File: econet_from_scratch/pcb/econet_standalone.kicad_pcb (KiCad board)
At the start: 2 copper layers, 100 x 100 mm, 24 parts, among them CON1 jtag, U1 Econet, U2 SN65C1168, U3 LM319, U4 XC9572XL, U5 MCP1700T-3302E/MB

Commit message: More progress on econet_from_scratch
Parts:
- removed CON1: jtag, Pin_Headers:Pin_Header_Straight_2x05_Pitch2.54mm
- added C7: 100n, Capacitors_SMD:C_0805_HandSoldering, F.Cu at (166.1, 52.1)
- added EXT: ext, Pin_Headers:Pin_Header_Straight_2x05_Pitch2.54mm, F.Cu at (150.4, 75.9)
- added JTAG: jtag, Pin_Headers:Pin_Header_Straight_2x05_Pitch2.54mm, F.Cu at (150.0, 50.4)
- moved C4 60.0 mm to (169.1, 69.9)
- moved C5 60.0 mm to (165.6, 73.6)
- moved U5 60.0 mm to (169.3, 73.6)
- moved C3 54.4 mm to (147.7, 59.3), turned to 270 degrees
- moved U4 51.5 mm to (156.0, 60.2), turned to 270 degrees
- moved U2 49.0 mm to (173.0, 52.0), turned to 90 degrees
- moved C2 39.7 mm to (154.1, 68.7), turned to 180 degrees
- moved U1 27.8 mm to (190.2, 52.2)
- moved C1 25.2 mm to (180.2, 69.9)
- moved R1 25.2 mm to (180.2, 72.0)
- moved R10 25.2 mm to (193.5, 75.7)
- moved R12 25.2 mm to (180.1, 78.2)
- moved R2 25.2 mm to (180.2, 67.7)
- moved R4 25.2 mm to (197.0, 75.2)
- moved R5 25.2 mm to (193.5, 71.7)
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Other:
- board size 100 x 100 mm -> 55 x 40 mm
- board text added: "econet_from_scratch Phillip Pearson 2017"

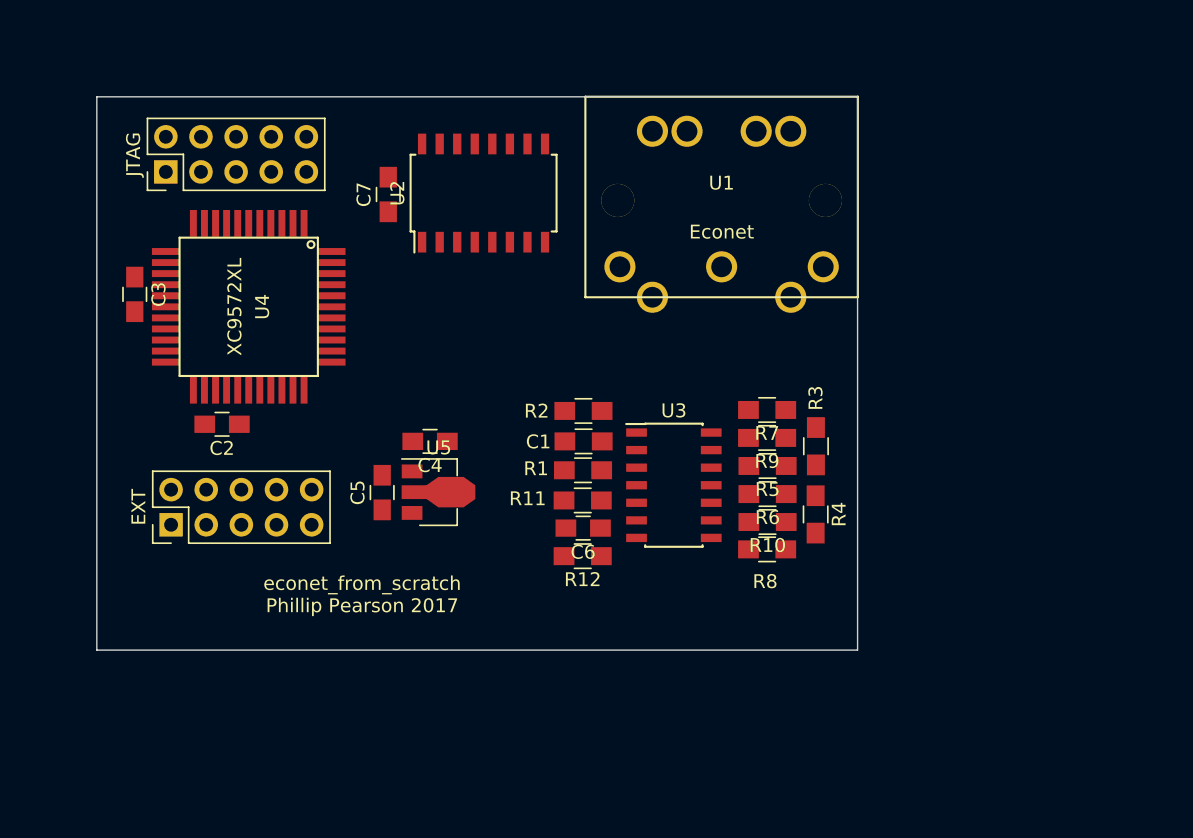
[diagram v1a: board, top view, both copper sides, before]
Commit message: Progress on econet_from_scratch; it's nearly all routed
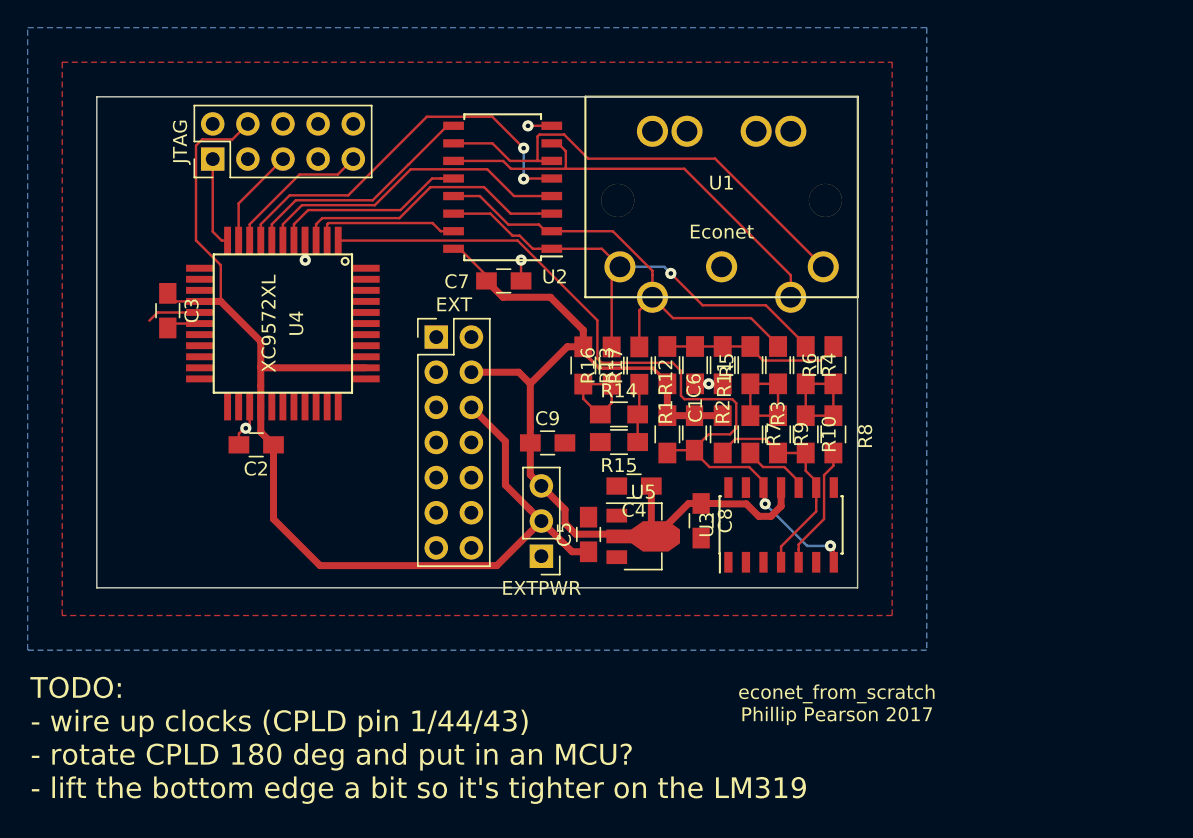
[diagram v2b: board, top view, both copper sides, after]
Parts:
- removed the EXT at (150.4, 75.9)
- added C8: 100n, Capacitors_SMD:C_0805_HandSoldering, F.Cu at (188.7, 75.7)
- added C9: 10u, Capacitors_SMD:C_0805_HandSoldering, F.Cu at (177.6, 70.0)
- added EXT: ext, Pin_Headers:Pin_Header_Straight_2x07_Pitch2.54mm, F.Cu at (169.5, 62.4)
- added EXTPWR: ext pwr, Pin_Headers:Pin_Header_Straight_1x03_Pitch2.54mm, F.Cu at (177.1, 78.2)
- added R13: 1k, Resistors_SMD:R_0805_HandSoldering, F.Cu at (180.2, 64.4)
- added R14: 220R, Resistors_SMD:R_0805_HandSoldering, F.Cu at (182.8, 68.0)
- added R15: 1k, Resistors_SMD:R_0805_HandSoldering, F.Cu at (182.8, 70.0)
- added R16: 56R, Resistors_SMD:R_0805_HandSoldering, F.Cu at (182.2, 64.4)
- added R17: 56R, Resistors_SMD:R_0805_HandSoldering, F.Cu at (184.2, 64.4)
- moved C5 15.2 mm to (180.6, 76.6)
- moved U5 15.1 mm to (184.1, 76.8)
- moved C4 15.1 mm to (183.8, 73.1)
- moved R11 11.2 mm to (190.2, 69.4), turned to 90 degrees
- moved R4 10.8 mm to (196.2, 64.4)
- moved R12 10.7 mm to (186.2, 69.4), turned to 90 degrees
- moved R2 10.6 mm to (190.2, 64.4), turned to 270 degrees
- moved C6 10.6 mm to (188.2, 69.3), turned to 90 degrees
- moved R6 10.5 mm to (198.2, 64.4), turned to 90 degrees
- moved C7 10.4 mm to (174.4, 58.3), turned to 0 degrees
- moved C1 9.76 mm to (188.2, 64.4), turned to 270 degrees
- moved R1 9.75 mm to (186.2, 64.4), turned to 90 degrees
- moved R8 9.60 mm to (198.2, 69.4), turned to 270 degrees
- moved U3 8.26 mm to (194.5, 76.0), turned to 90 degrees
- moved R5 7.39 mm to (192.2, 64.4), turned to 90 degrees
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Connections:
- U3 pad 11: GND -> 5V
- U4 pad 1: _default -> collision_detect
- U4 pad 2: _default -> econet_data_D
- U4 pad 3: _default -> econet_data_R
- U4 pad 5: _default -> econet_clock_DE
- U4 pad 6: _default -> econet_data_DE
- U4 pad 7: _default -> econet_clock_D
- U4 pad 8: _default -> econet_clock_R
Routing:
- net 3V3: track 0.00 -> 82.4 mm
- net 5V: track 0.00 -> 67.9 mm
- net collision_detect: track 0.00 -> 58.9 mm, vias 0 -> 2
- net econet_data_line_P: track 0.00 -> 36.2 mm, vias 0 -> 1
- net econet_clock_line_M: track 0.00 -> 34.1 mm
- net econet_data_line_M: track 0.00 -> 33.1 mm
- net econet_clock_line_P: track 0.00 -> 31.9 mm
- net econet_clock_R: track 0.00 -> 28.6 mm, vias 0 -> 2
- net econet_data_DE: track 0.00 -> 23.1 mm
- net econet_data_R: track 0.00 -> 20.1 mm
- net econet_clock_D: track 0.00 -> 17.3 mm
- net econet_centre: track 0.00 -> 16.2 mm
- net econet_clock_DE: track 0.00 -> 14.1 mm
- net GND: track 0.00 -> 13.6 mm, vias 0 -> 5
- net cd_vdiv_2v: track 0.00 -> 13.0 mm
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- added copper zone on B.Cu, net GND
- added copper zone on F.Cu, net GND
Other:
- board size 55 x 40 mm -> 55 x 35.5 mm
- board text added: "TODO: - wire up clocks (CPLD pin 1/44/43) - rotate CPLD 180 deg and put in an MCU? - lift the bottom edge a bit so it's tighter on the LM319"

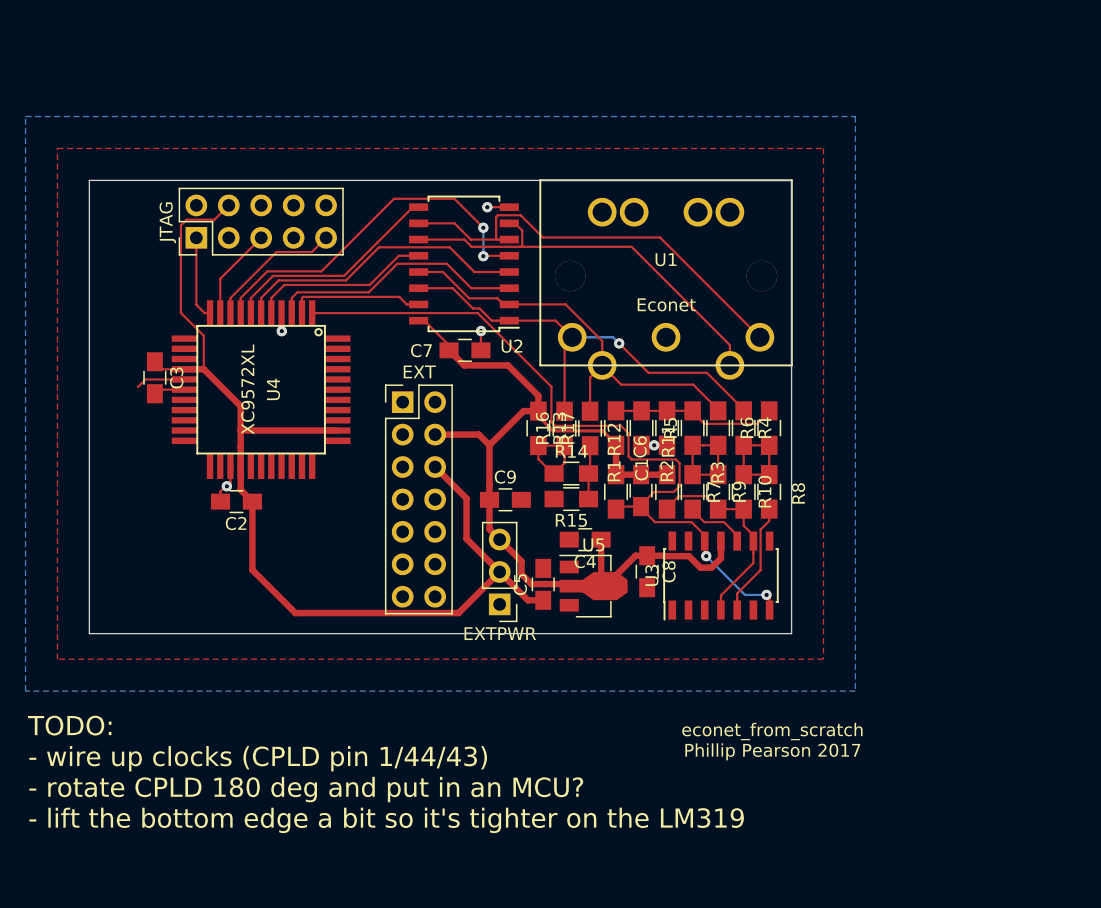
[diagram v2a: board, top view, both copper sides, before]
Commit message: econet_from_scratch passes DRC, and now includes an ATSAMD21E
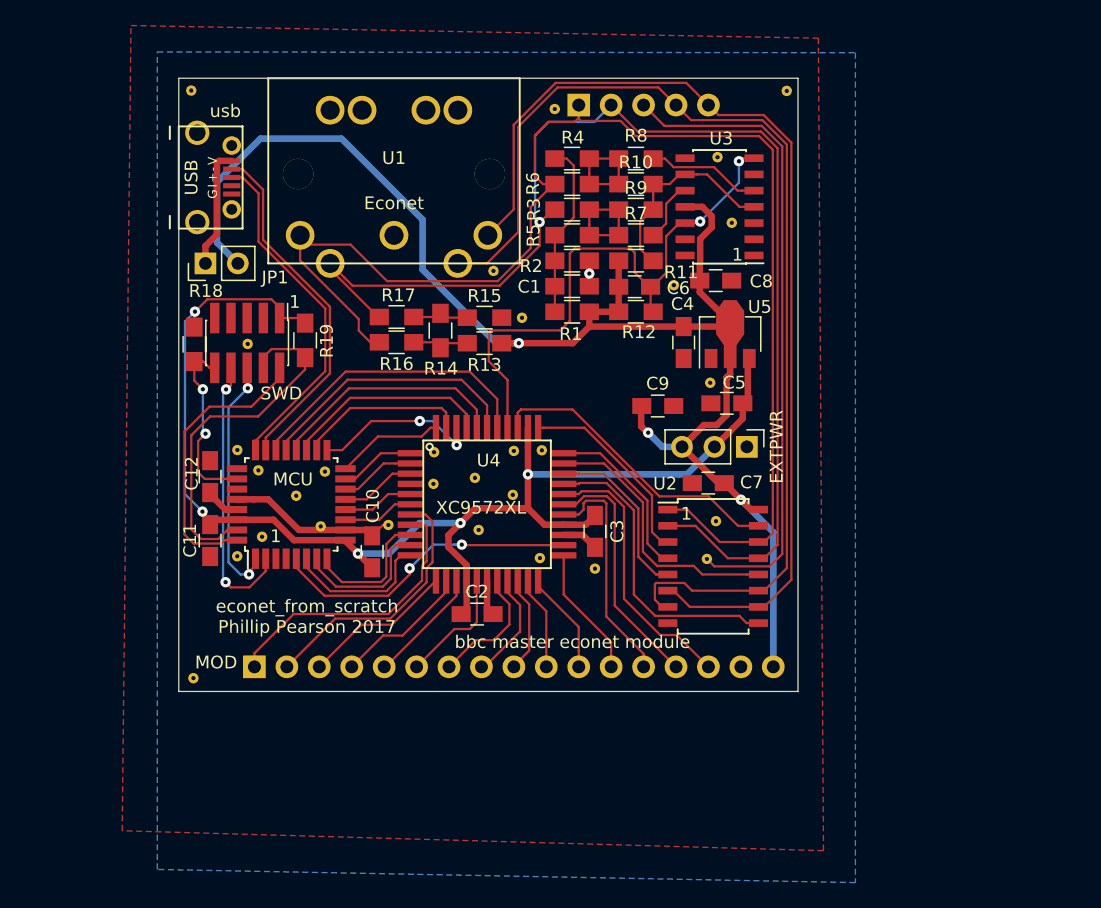
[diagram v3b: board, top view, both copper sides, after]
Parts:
- removed EXT: ext, Pin_Headers:Pin_Header_Straight_2x07_Pitch2.54mm
- removed JTAG: jtag, Pin_Headers:Pin_Header_Straight_2x05_Pitch2.54mm
- added C10: 100n, Capacitors_SMD:C_0805_HandSoldering, F.Cu at (167.2, 74.1)
- added C11: 100n, Capacitors_SMD:C_0805_HandSoldering, F.Cu at (154.5, 73.2)
- added C12: 1u, Capacitors_SMD:C_0805_HandSoldering, F.Cu at (154.5, 68.2)
- added JP1: USB power, Pin_Headers:Pin_Header_Straight_1x02_Pitch2.54mm, F.Cu at (154.1, 51.5)
- added MCU: ATSAMD21E18A, Housings_QFP:TQFP-32_7x7mm_Pitch0.8mm, F.Cu at (160.8, 70.4)
- added MOD: bbc master econet module, myelin-kicad:bbc_master_econet_module, F.Cu at (179.5, 61.1)
- added R18: 10k, Resistors_SMD:R_0805_HandSoldering, F.Cu at (153.2, 57.8)
- added R19: 1k, Resistors_SMD:R_0805_HandSoldering, F.Cu at (161.9, 57.5)
- added SWD: swd, Pin_Headers:Pin_Header_Straight_2x05_Pitch1.27mm_SMD, F.Cu at (157.4, 57.7)
- added USB: usb, myelin-kicad:micro_usb_b_smd_molex, F.Cu at (154.0, 44.8)
- added staple_single1: , myelin-kicad:via_single, F.Cu at (171.9, 68.8)
- added staple_single10: , myelin-kicad:via_single, F.Cu at (153.0, 38.0)
- added staple_single11: , myelin-kicad:via_single, F.Cu at (156.6, 66.1)
- added staple_single12: , myelin-kicad:via_single, F.Cu at (168.4, 72.0)
- added staple_single13: , myelin-kicad:via_single, F.Cu at (184.6, 75.4)
- added staple_single14: , myelin-kicad:via_single, F.Cu at (193.6, 60.9)
- added staple_single15: , myelin-kicad:via_single, F.Cu at (190.8, 53.2)
- added staple_single16: , myelin-kicad:via_single, F.Cu at (193.4, 74.7)
- added staple_single17: , myelin-kicad:via_single, F.Cu at (157.4, 57.8)
- added staple_single18: , myelin-kicad:via_single, F.Cu at (178.9, 55.8)
- added staple_single19: , myelin-kicad:via_single, F.Cu at (156.6, 74.4)
- added staple_single2: , myelin-kicad:via_single, F.Cu at (172.0, 66.3)
- added staple_single20: , myelin-kicad:via_single, F.Cu at (194.2, 43.2)
- added staple_single21: , myelin-kicad:via_single, F.Cu at (195.3, 48.3)
- added staple_single22: , myelin-kicad:via_single, F.Cu at (176.7, 52.1)
- added staple_single23: , myelin-kicad:via_single, F.Cu at (181.4, 39.4)
- added staple_single24: , myelin-kicad:via_single, F.Cu at (194.1, 71.7)
- added staple_single25: , myelin-kicad:via_single, F.Cu at (178.2, 66.2)
- added staple_single26: , myelin-kicad:via_single, F.Cu at (163.1, 72.1)
- added staple_single27: , myelin-kicad:via_single, F.Cu at (161.2, 69.7)
- added staple_single28: , myelin-kicad:via_single, F.Cu at (178.2, 69.6)
- added staple_single29: , myelin-kicad:via_single, F.Cu at (175.5, 72.4)
- added staple_single3: , myelin-kicad:via_single, F.Cu at (180.3, 74.6)
- added staple_single30: , myelin-kicad:via_single, F.Cu at (175.2, 68.3)
- added staple_single4: , myelin-kicad:via_single, F.Cu at (180.4, 66.1)
- added staple_single5: , myelin-kicad:via_single, F.Cu at (158.5, 72.9)
- added staple_single6: , myelin-kicad:via_single, F.Cu at (158.2, 67.7)
- added staple_single7: , myelin-kicad:via_single, F.Cu at (163.4, 67.8)
- added staple_single8: , myelin-kicad:via_single, F.Cu at (153.2, 84.0)
- added staple_single9: , myelin-kicad:via_single, F.Cu at (199.6, 38.0)
- moved C3 36.5 mm to (184.6, 72.5)
- moved U2 30.7 mm to (193.9, 75.2), turned to 0 degrees
- moved U3 28.9 mm to (194.4, 47.1), turned to 180 degrees
- moved R8 28.1 mm to (187.8, 43.3), turned to 0 degrees
- moved R6 26.2 mm to (182.8, 43.3), turned to 180 degrees
- moved R10 25.5 mm to (187.8, 45.3), turned to 0 degrees
- moved C8 23.4 mm to (194.1, 52.9), turned to 0 degrees
- moved R4 23.4 mm to (182.8, 45.3), turned to 0 degrees
- moved R9 23.0 mm to (187.8, 47.3), turned to 0 degrees
- moved EXTPWR 23.0 mm to (196.5, 65.9), turned to 270 degrees
- moved U1 22.8 mm to (168.9, 44.2)
- moved U5 22.3 mm to (195.2, 57.5), turned to 90 degrees
- moved C7 21.7 mm to (193.5, 68.7), turned to 180 degrees
- moved C2 20.8 mm to (175.4, 79.0), turned to 0 degrees
- moved R7 20.6 mm to (187.8, 49.3), turned to 0 degrees
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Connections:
- net econet_clock_line_M renamed econet_clock_line_N
- net econet_data_line_M renamed econet_data_line_N
- U4 pad 1: collision_detect -> PA14
- U4 pad 12: _default -> nADLC
- U4 pad 13: _default -> PHI2
- U4 pad 14: _default -> A0
- U4 pad 16: _default -> A1
- U4 pad 18: _default -> D0
- U4 pad 19: _default -> D1
- U4 pad 2: econet_data_D -> PA11
- U4 pad 20: _default -> D2
- U4 pad 21: _default -> D3
- U4 pad 22: _default -> D4
- U4 pad 23: _default -> D5
- U4 pad 27: _default -> D6
- U4 pad 28: _default -> D7
- U4 pad 29: _default -> nRESET
- U4 pad 3: econet_data_R -> PA10
- U4 pad 30: _default -> econet_clock_D
- U4 pad 31: _default -> econet_clock_R
- U4 pad 32: _default -> econet_clock_DE
- U4 pad 33: _default -> econet_data_DE
- U4 pad 34: _default -> econet_data_R
- U4 pad 36: _default -> econet_data_D
- U4 pad 37: _default -> collision_detect
- U4 pad 38: _default -> PA23
- U4 pad 39: _default -> PA22
- U4 pad 40: _default -> PA19
- U4 pad 41: _default -> PA18
- U4 pad 42: _default -> PA16
- U4 pad 43: _default -> PA17
- U4 pad 44: _default -> PA15
- U4 pad 5: econet_clock_DE -> PA09
- U4 pad 6: econet_data_DE -> PA08
- U4 pad 7: econet_clock_D -> RnW
- U4 pad 8: econet_clock_R -> nNETINT
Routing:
- net econet_data_line_P: track 36.2 -> 104.7 mm, vias 1 -> 0
- net econet_data_line_N: track 33.1 -> 97.7 mm, vias 0 -> 1
- net GND: track 13.6 -> 72.8 mm, vias 5 -> 1
- net econet_clock_line_P: track 31.9 -> 86.8 mm
- net 5V: track 67.9 -> 120.1 mm, vias 0 -> 3
- net econet_clock_line_N: track 34.1 -> 79.9 mm
- net SWCLK: track 0.00 -> 29.8 mm
- net USBDP: track 0.00 -> 28.0 mm
- net USBDM: track 0.00 -> 27.8 mm
- net cpld_TDO: track 0.00 -> 24.5 mm, vias 0 -> 2
- net SWDIO: track 0.00 -> 23.6 mm
- net PA23: track 0.00 -> 23.4 mm
- net mcu_RXD: track 0.00 -> 22.8 mm, vias 0 -> 2
- net nNETINT: track 0.00 -> 22.3 mm
- net nRESET: track 0.00 -> 21.3 mm
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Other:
- board size 55 x 35.5 mm -> 48.5 x 48 mm
- board text added: "1"
- board text removed: "TODO: - wire up clocks (CPLD pin 1/44/43) - rotate CPLD 180 deg and put in an MCU? - lift the bottom edge a bit so it's tighter on the LM319"

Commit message: econet_from_scratch: Ready to send off
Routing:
- net GND: track 72.8 -> 76.9 mm
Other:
- board text added: ""Econet from scratch" http://myelin.nz/acorn/ecostd Phillip Pearson Copyright 2017 Google LLC"
- board text added: "github.com/google/myelin-acorn-electron-hardware"
